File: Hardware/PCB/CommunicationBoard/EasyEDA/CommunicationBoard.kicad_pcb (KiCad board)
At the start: 4 copper layers, 60 x 60 mm, 54 parts, among them J1 SWD, J2 Conn_01x07, J3 Conn_01x07, J4 Conn_01x07, J6 USB_C_Receptacle_USB2.0, J7 TWELITER, SW1 nRF_RESET, SW2 nRF_DFU, SW3 TWE_CLEAR, SW4 TWE_RESET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

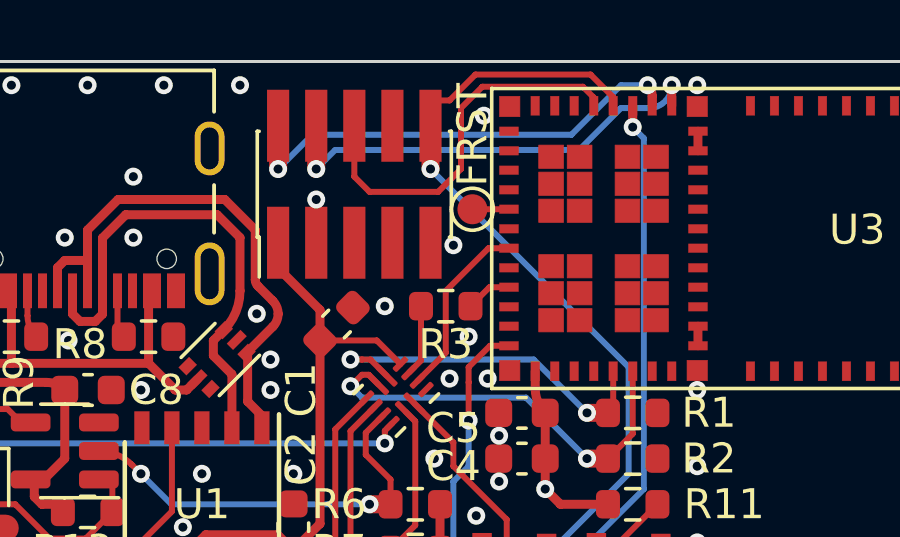
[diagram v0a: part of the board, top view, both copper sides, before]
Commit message: 書き込み用変換基板を作成、0.5/0.2mmビアを排除
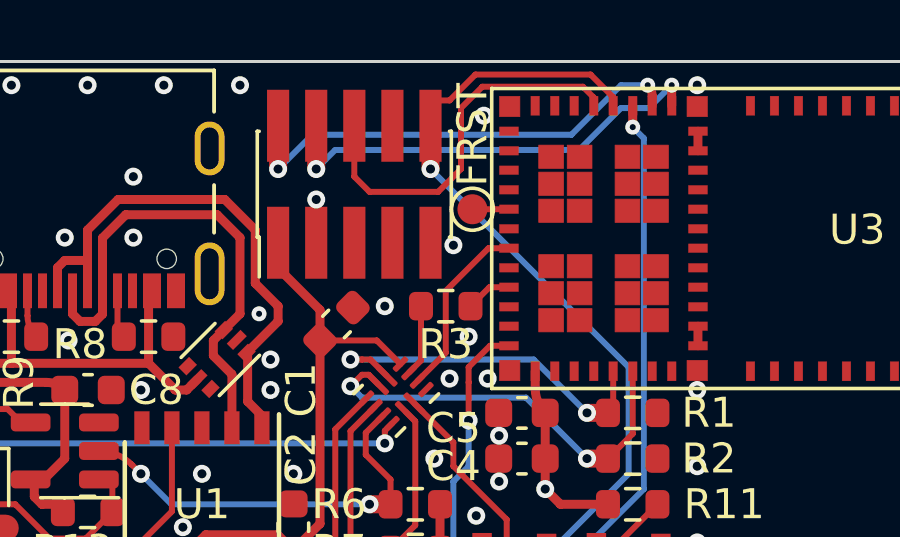
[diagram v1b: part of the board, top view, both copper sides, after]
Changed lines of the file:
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@@
   (gr_line (start 181 76) (end 181 78.5) (layer "Dwgs.User") (width 0.15))
   (gr_line (start 181 71.5) (end 181.5 73) (layer "Dwgs.User") (width 0.15))
-  (gr_line (start 164.4 70.3) (end 160.7 70.3) (layer "Dwgs.User") (width 0.05))
   (gr_line (start 181 78.5) (end 181.5 77) (layer "Dwgs.User") (width 0.15))
   (gr_line (start 181 71.5) (end 180.5 73) (layer "Dwgs.User") (width 0.15))
@@
   (via (at 141.19 108.89) (size 0.6) (drill 0.3) (layers "F.Cu" "B.Cu") (free) (net 1))
   (via (at 143.476 91.618) (size 0.6) (drill 0.3) (layers "F.Cu" "B.Cu") (free) (net 1))
-  (via (at 149.3688 78.41) (size 0.6) (drill 0.3) (layers "F.Cu" "B.Cu") (free) (net 1))
   (via (at 144.746 89.586) (size 0.6) (drill 0.3) (layers "F.Cu" "B.Cu") (free) (net 1))
   (via (at 158.97 108.89) (size 0.6) (drill 0.3) (layers "F.Cu" "B.Cu") (free) (net 1))
@@
   (via (at 136.618 74.6) (size 0.6) (drill 0.3) (layers "F.Cu" "B.Cu") (free) (net 1))
   (via (at 143.984 98.73) (size 0.6) (drill 0.3) (layers "F.Cu" "B.Cu") (free) (net 1))
+  (via (at 149.445 78.41) (size 0.5) (drill 0.2) (layers "F.Cu" "B.Cu") (free) (net 1))
   (via (at 141.952 96.444) (size 0.6) (drill 0.3) (layers "F.Cu" "B.Cu") (free) (net 1))
   (via (at 149.826 79.934) (size 0.6) (drill 0.3) (layers "F.Cu" "B.Cu") (free) (net 1))
@@
   (segment (start 162.55 71.475) (end 162.55 71.154546) (width 0.3) (layer "F.Cu") (net 6))
   (via (at 150.08 73.584) (size 0.6) (drill 0.3) (layers "F.Cu" "B.Cu") (net 6))
-  (via (at 162.399 70.79) (size 0.6) (drill 0.3) (layers "F.Cu" "B.Cu") (net 6))
+  (via (at 162.399 70.79) (size 0.5) (drill 0.2) (layers "F.Cu" "B.Cu") (net 6))
   (arc (start 162.55 71.154546) (mid 162.510756 70.957255) (end 162.399 70.79) (width 0.3) (layer "F.Cu") (net 6))
   (segment (start 161.51 70.79) (end 159.859 72.441) (width 0.2) (layer "B.Cu") (net 6))
-  (segment (start 161.51 70.79) (end 162.399 70.79) (width 0.2) (layer "B.Cu") (net 6))
+  (segment (start 162.399 70.79) (end 161.51 70.79) (width 0.2) (layer "B.Cu") (net 6))
   (segment (start 159.859 72.441) (end 151.223 72.441) (width 0.2) (layer "B.Cu") (net 6))
   (segment (start 151.223 72.441) (end 150.08 73.584) (width 0.2) (layer "B.Cu") (net 6))
   (segment (start 151.35 72.142) (end 151.35 73.584) (width 0.6) (layer "F.Cu") (net 7))
   (segment (start 163.2 71.475) (end 163.2 70.79) (width 0.3) (layer "F.Cu") (net 7))
-  (via (at 163.2 70.79) (size 0.6) (drill 0.3) (layers "F.Cu" "B.Cu") (net 7))
+  (via (at 163.2 70.79) (size 0.5) (drill 0.2) (layers "F.Cu" "B.Cu") (net 7))
   (via (at 151.35 73.584) (size 0.6) (drill 0.3) (layers "F.Cu" "B.Cu") (net 7))
-  (segment (start 161.51 71.552) (end 162.438 71.552) (width 0.2) (layer "B.Cu") (net 7))
   (segment (start 151.985 72.949) (end 151.35 73.584) (width 0.2) (layer "B.Cu") (net 7))
   (segment (start 161.51 71.552) (end 160.113 72.949) (width 0.2) (layer "B.Cu") (net 7))
+  (segment (start 163.2 70.79) (end 162.438 71.552) (width 0.2) (layer "B.Cu") (net 7))
   (segment (start 160.113 72.949) (end 151.985 72.949) (width 0.2) (layer "B.Cu") (net 7))
-  (arc (start 162.438 71.552) (mid 162.976815 71.328815) (end 163.2 70.79) (width 0.2) (layer "B.Cu") (net 7))
+  (segment (start 162.438 71.552) (end 161.51 71.552) (width 0.2) (layer "B.Cu") (net 7))
   (segment (start 156.176 71.552) (end 156.8872 70.8408) (width 0.2) (layer "F.Cu") (net 8))
   (segment (start 156.176 73.584) (end 156.176 71.552) (width 0.2) (layer "F.Cu") (net 8))
@@
   (segment (start 144.726 77.643) (end 144.726 78.961) (width 0.2) (layer "F.Cu") (net 25))
   (segment (start 144.726 78.961) (end 144.937 79.172) (width 0.2) (layer "F.Cu") (net 25))
+  (segment (start 150.08 78.156) (end 149.318 77.394) (width 0.3) (layer "F.Cu") (net 26))
+  (segment (start 142.726 76.874) (end 142.968 76.632) (width 0.3) (layer "F.Cu") (net 26))
+  (segment (start 148.302 74.6) (end 144.746 74.6) (width 0.3) (layer "F.Cu") (net 26))
+  (segment (start 142.726 77.643) (end 142.726 76.874) (width 0.3) (layer "F.Cu") (net 26))
+  (segment (start 142.968 76.632) (end 143.726 76.632) (width 0.3) (layer "F.Cu") (net 26))
+  (segment (start 149.318 77.394) (end 149.318 75.616) (width 0.3) (layer "F.Cu") (net 26))
+  (segment (start 149.54 81.807) (end 149.064 81.331) (width 0.3) (layer "F.Cu") (net 26))
   (segment (start 143.726 75.62) (end 143.726 77.643) (width 0.3) (layer "F.Cu") (net 26))
-  (segment (start 142.726 76.874) (end 142.968 76.632) (width 0.3) (layer "F.Cu") (net 26))
-  (segment (start 142.726 77.643) (end 142.726 76.874) (width 0.3) (layer "F.Cu") (net 26))
-  (segment (start 149.318 77.267) (end 149.318 75.616) (width 0.3) (layer "F.Cu") (net 26))
-  (segment (start 142.968 76.632) (end 143.726 76.632) (width 0.3) (layer "F.Cu") (net 26))
-  (segment (start 149.029111 79.713029) (end 149.90171 78.84043) (width 0.3) (layer "F.Cu") (net 26))
-  (segment (start 148.302 74.6) (end 144.746 74.6) (width 0.3) (layer "F.Cu") (net 26))
-  (segment (start 149.54 81.807) (end 149.064 81.331) (width 0.3) (layer "F.Cu") (net 26))
+  (segment (start 149.318 75.616) (end 148.302 74.6) (width 0.3) (layer "F.Cu") (net 26))
+  (segment (start 149.029111 79.713029) (end 150.08 78.66214) (width 0.3) (layer "F.Cu") (net 26))
   (segment (start 144.746 74.6) (end 143.726 75.62) (width 0.3) (layer "F.Cu") (net 26))
-  (segment (start 149.900394 77.976394) (end 149.407803 77.483803) (width 0.3) (layer "F.Cu") (net 26))
   (segment (start 149.064 81.331) (end 149.064 79.747918) (width 0.3) (layer "F.Cu") (net 26))
-  (segment (start 149.318 75.616) (end 148.302 74.6) (width 0.3) (layer "F.Cu") (net 26))
   (segment (start 149.064 79.747918) (end 149.029111 79.713029) (width 0.3) (layer "F.Cu") (net 26))
   (segment (start 149.54 82.21) (end 149.54 81.807) (width 0.3) (layer "F.Cu") (net 26))
-  (arc (start 149.407803 77.483803) (mid 149.341339 77.384333) (end 149.318 77.267) (width 0.3) (layer "F.Cu") (net 26))
-  (arc (start 150.08 78.41) (mid 150.033322 78.175334) (end 149.900394 77.976394) (width 0.3) (layer "F.Cu") (net 26))
-  (arc (start 149.90171 78.84043) (mid 150.033664 78.642947) (end 150.08 78.41) (width 0.3) (layer "F.Cu") (net 26))
+  (segment (start 150.08 78.156) (end 150.08 78.66214) (width 0.3) (layer "F.Cu") (net 26))
   (segment (start 148.54 80.426) (end 147.921 79.807) (width 0.3) (layer "F.Cu") (net 27))
   (segment (start 143.476 78.664) (end 143.984 78.664) (width 0.3) (layer "F.Cu") (net 27))
   (segment (start 147.921 79.30086) (end 148.268971 78.952889) (width 0.3) (layer "F.Cu") (net 27))
-  (segment (start 148.81 75.87) (end 148.81 77.64673) (width 0.3) (layer "F.Cu") (net 27))
   (segment (start 144.226 78.422) (end 143.984 78.664) (width 0.3) (layer "F.Cu") (net 27))
   (segment (start 148.048 75.108) (end 148.81 75.87) (width 0.3) (layer "F.Cu") (net 27))
   (segment (start 147.921 79.807) (end 147.921 79.30086) (width 0.3) (layer "F.Cu") (net 27))
+  (segment (start 148.81 78.41186) (end 148.268971 78.952889) (width 0.3) (layer "F.Cu") (net 27))
   (segment (start 144.226 77.643) (end 144.226 75.882) (width 0.3) (layer "F.Cu") (net 27))
+  (segment (start 148.81 75.87) (end 148.81 78.41186) (width 0.3) (layer "F.Cu") (net 27))
   (segment (start 144.226 77.643) (end 144.226 78.422) (width 0.3) (layer "F.Cu") (net 27))
   (segment (start 148.54 82.21) (end 148.54 80.426) (width 0.3) (layer "F.Cu") (net 27))
@@
   (segment (start 144.226 75.882) (end 145 75.108) (width 0.3) (layer "F.Cu") (net 27))
   (segment (start 145 75.108) (end 148.048 75.108) (width 0.3) (layer "F.Cu") (net 27))
-  (arc (start 148.81 77.64673) (mid 148.669391 78.353618) (end 148.268971 78.952889) (width 0.3) (layer "F.Cu") (net 27))
   (segment (start 141.726 77.643) (end 141.726 78.474293) (width 0.2) (layer "F.Cu") (net 28))
   (arc (start 141.726 78.474293) (mid 141.801109 78.851889) (end 142.015 79.172) (width 0.2) (layer "F.Cu") (net 28))
@@
   (segment (start 161.455 86.03) (end 160.689 86.03) (width 0.2) (layer "F.Cu") (net 41))
   (via (at 160.689 87.046) (size 0.6) (drill 0.3) (layers "F.Cu" "B.Cu") (net 41))
-  (via (at 161.9 72.187) (size 0.6) (drill 0.3) (layers "F.Cu" "B.Cu") (net 41))
+  (via (at 161.9 72.187) (size 0.5) (drill 0.2) (layers "F.Cu" "B.Cu") (net 41))
   (segment (start 162.272 84.252) (end 162.272 72.559) (width 0.2) (layer "B.Cu") (net 41))
   (segment (start 162.272 72.559) (end 161.9 72.187) (width 0.2) (layer "B.Cu") (net 41))
